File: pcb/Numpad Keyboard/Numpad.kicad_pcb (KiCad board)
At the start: 2 copper layers, 82.4 x 128 mm, 65 parts, among them J1 Conn_01x04, J2 Conn_01x04, U1 MAX7301ATL+, U2 IS31FL3743-QF, U3 IS31FL3743-QF

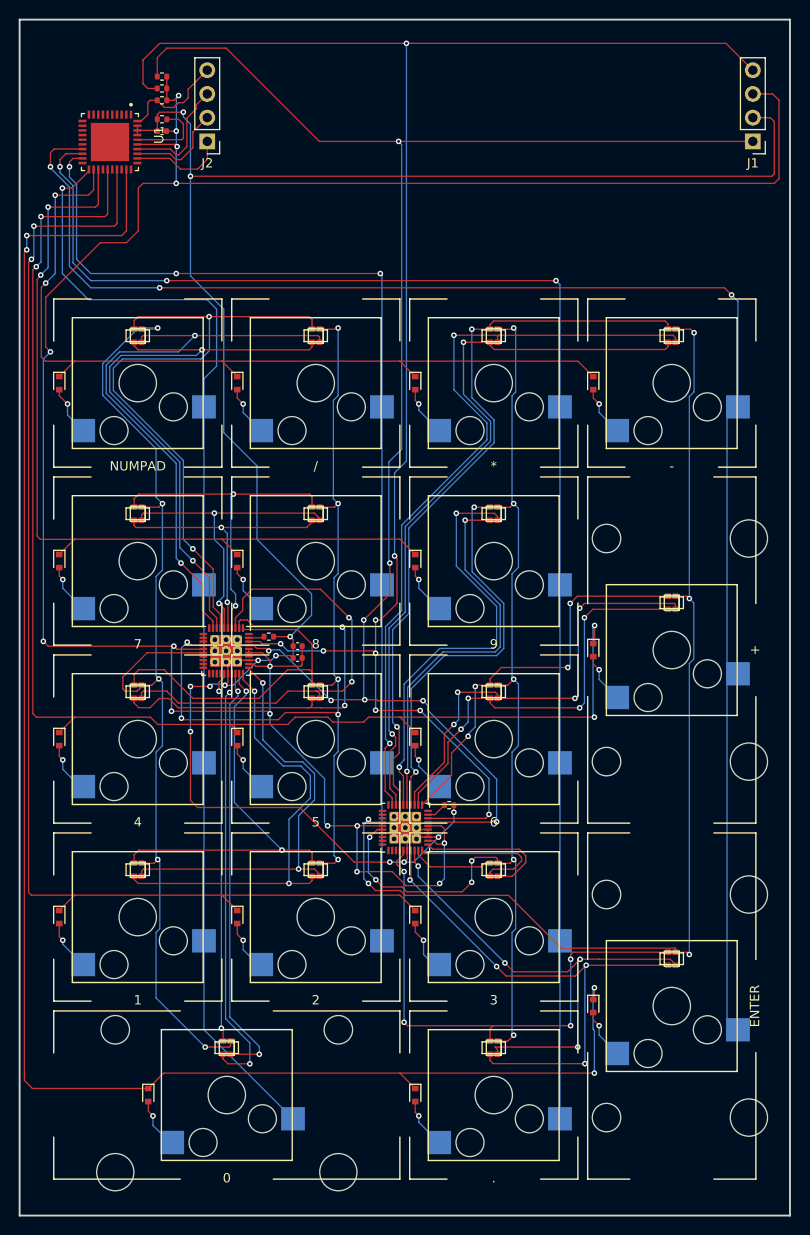
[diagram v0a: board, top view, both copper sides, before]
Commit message: Solved conflict of resistor with switch
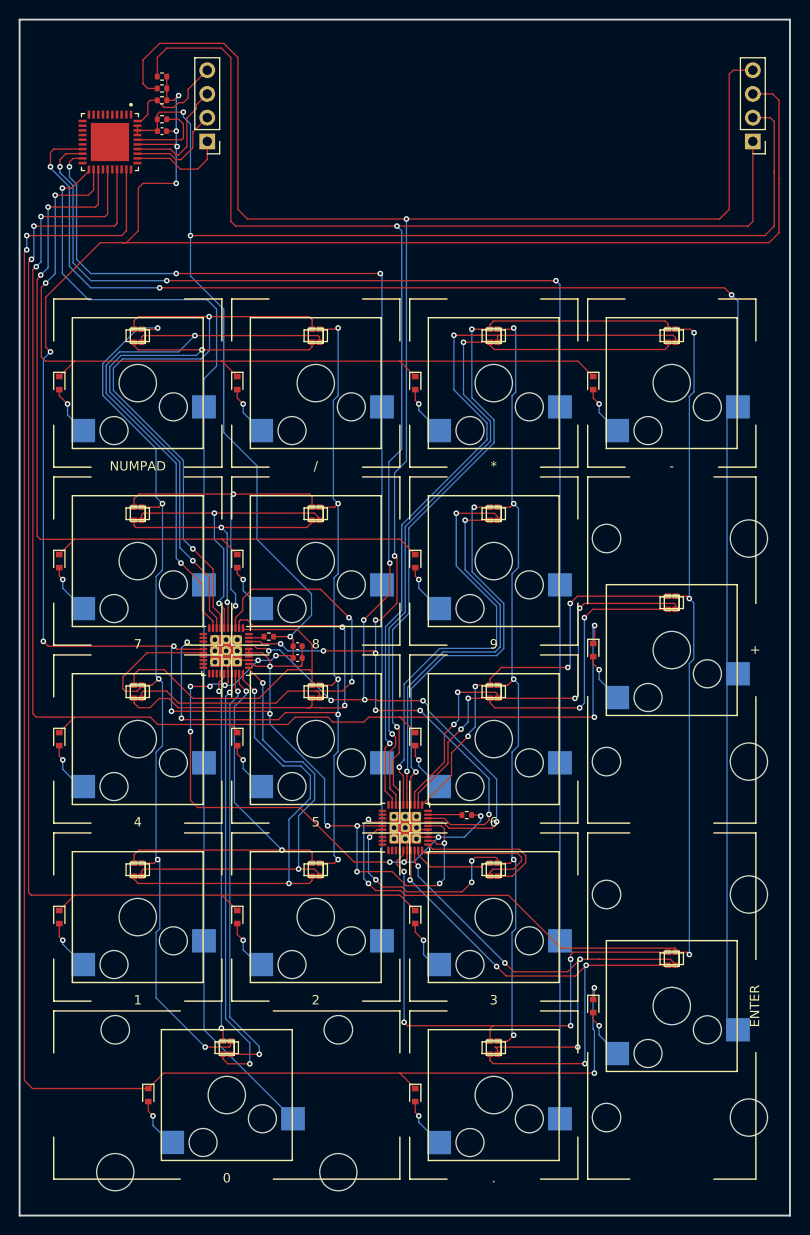
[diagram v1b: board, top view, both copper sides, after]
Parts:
- moved R3 2.16 mm to (69.7, 108.0)
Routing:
- net Net-(J1-Pad1): track 176.8 -> 191.3 mm
- net Net-(J1-Pad4): track 184.6 -> 197.8 mm
- net Net-(C1-Pad1): track 251.3 -> 263.1 mm
- net Net-(C1-Pad2): track 219.0 -> 227.8 mm
- net Net-(R3-Pad2): track 2.17 -> 3.66 mm
